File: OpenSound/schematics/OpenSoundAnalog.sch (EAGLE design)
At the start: 60 parts, among them IC2 QUAD_OPAMPD, IC3 TL072D, Q1 BC846, Q2 BC846, Q301 BC846, Q701 BC846

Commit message: changed layout and added Spark Photon footprint
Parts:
- removed CV_A, CV_B: CON-LUMBERG_1502_03, Rebel:CON-LUMBERG_1502_03
- removed IC3: TL072D, linear:TL072D
- removed R1, R3, R4: 1K, resistor:R-EU_R0603
- removed R2: 100R, resistor:R-EU_R0603
- removed R5: 100K, resistor:R-EU_R0603
- removed R6: 10K, resistor:R-EU_R0603
- removed R7: 1M, resistor:R-EU_R0603
- removed R8: 1k, Rebel:R-EU_0603
- removed SV1, SV2: (no value), con-lsta:FE12-1
- removed U$1: MCP4922-E/P, Rebel:MCP4922-E/P
- added CVI1, CVI2: THONKICONN, Rebel:THONKICONN
- added IC1: MCP4822-E/PSOIC8, Rebel:MCP4822-E/PSOIC8
- added R301: 240k, resistor:R-EU_R0603
- added R302: 51k, resistor:R-EU_R0603
- added R303: 33k, resistor:R-EU_R0603
- added R304, R903: 100R, resistor:R-EU_R0603
- added R801: 100K, resistor:R-EU_R0603
- added R802: 1M, resistor:R-EU_R0603
- added R803: 10K, resistor:R-EU_R0603
- added R901, R902, R904: 1K, resistor:R-EU_R0603
- added SPARK: SPARK_CORE, Spark:SPARK_CORECORE
- R504: value 100R -> 1k; device resistor:R-EU_R0603 -> Rebel:R-EU_0603
- renumbered D600 to D200, DAC1 to CVO1, DAC2 to CVO2, R10 to R202, R11 to R203, R604 to R204, R605 to R205, R9 to R201
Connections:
- new net N$12: IC2D.+IN, R301.1, R302.1
- new net N$15: IC2D.-IN, R303.1
- net +12V: now also IC2P.V+, R902.1; no longer IC3P.V+, R4.1
- net +3V3: now also IC1.VDD, R803.1, SPARK.3V3; no longer R6.1, SV1.10, SV1.12, U$1.VDD, U$1.VREFA, U$1.VREFB, U$1.~SHDN
- net +5V: now also SPARK.VIN; no longer SV2.1
- net -12V: now also IC2P.V-, R301.2; no longer IC3P.V-
- net A0: now also SPARK.A0; no longer SV2.12
- net A1: now also SPARK.A1; no longer SV2.11
- net A2: now also IC1.~CS, SPARK.A2; no longer SV2.10, U$1.~CS
- net A3: now also IC1.SCK, SPARK.A3; no longer SV2.9, U$1.SCK
- net A4: now also SPARK.A4; no longer SV2.8
- net A5: now also IC1.SDI, SPARK.A5; no longer SV2.7, U$1.SDI
- net A6: now also SPARK.DAC; no longer SV2.6
- net A7: now also SPARK.WKP; no longer SV2.5
- net D0: now also R901.1, SPARK.D0; no longer R1.1, SV1.1
- net D1: now also SPARK.D1; no longer SV1.2
- net D2: now also R803.2, SPARK.D2; no longer R6.2, SV1.3
- net D3: now also SPARK.D3; no longer SV1.4
- net D4: now also SPARK.D4; no longer SV1.5
- net D5: now also SPARK.D5; no longer SV1.6
- net D6: now also SPARK.D6; no longer SV1.7
- net D7: now also SPARK.D7; no longer SV1.8
- net DAC1: now also IC1.VOUTA; no longer U$1.VOUTA
- net DAC2: now also IC1.VOUTB, R303.2; no longer IC3B.+IN, U$1.VOUTB
- net GND: now also CVI1.4, CVI1.5, CVI2.4, CVI2.5, IC1.AVSS, IC1.~LDAC, IC2C.-IN, R802.2, R904.1, SPARK.GND@2, SPARK.GND@21; no longer CV_A.4, CV_A.5, CV_B.4, CV_B.5, IC3A.+IN, R3.1, R7.2, SV1.9, SV2.2, U$1.AVSS, U$1.~LDAC
- net N$10: now also R801.1; no longer R5.1
- net N$11: now also CVI1.3; no longer CV_A.3
- net N$13: now also IC2C.+IN; no longer IC3A.-IN
- net N$16: now also R504.1; no longer R8.1
- net N$17: now also R504.2; no longer R8.2
- net N$18: now also CVI2.3; no longer CV_B.3
- net N$2: now also R901.2; no longer R1.2
- net N$3: now also IC2D.OUT, R302.2, R304.1; no longer IC3B.-IN, IC3B.OUT, R504.1
- net N$32: now also R304.2; no longer R504.2
- net N$4: now also R902.2, R903.1; no longer R2.1, R4.2
- net N$5: now also R903.2, R904.2; no longer R2.2, R3.2
- net N$7: now also IC2C.OUT; no longer IC3A.OUT
- net N$9: now also R801.2, R802.1; no longer R5.2, R7.1
- net RESET: now also SPARK.!RST; no longer SV1.11
- net RX: now also SPARK.RX; no longer SV2.3
- net TX: now also SPARK.TX; no longer SV2.4
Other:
- moved on the sheet: D500, IC2A, Q1, Q2, Q301, Q701, R501, R502, R503, R504, R505, R601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

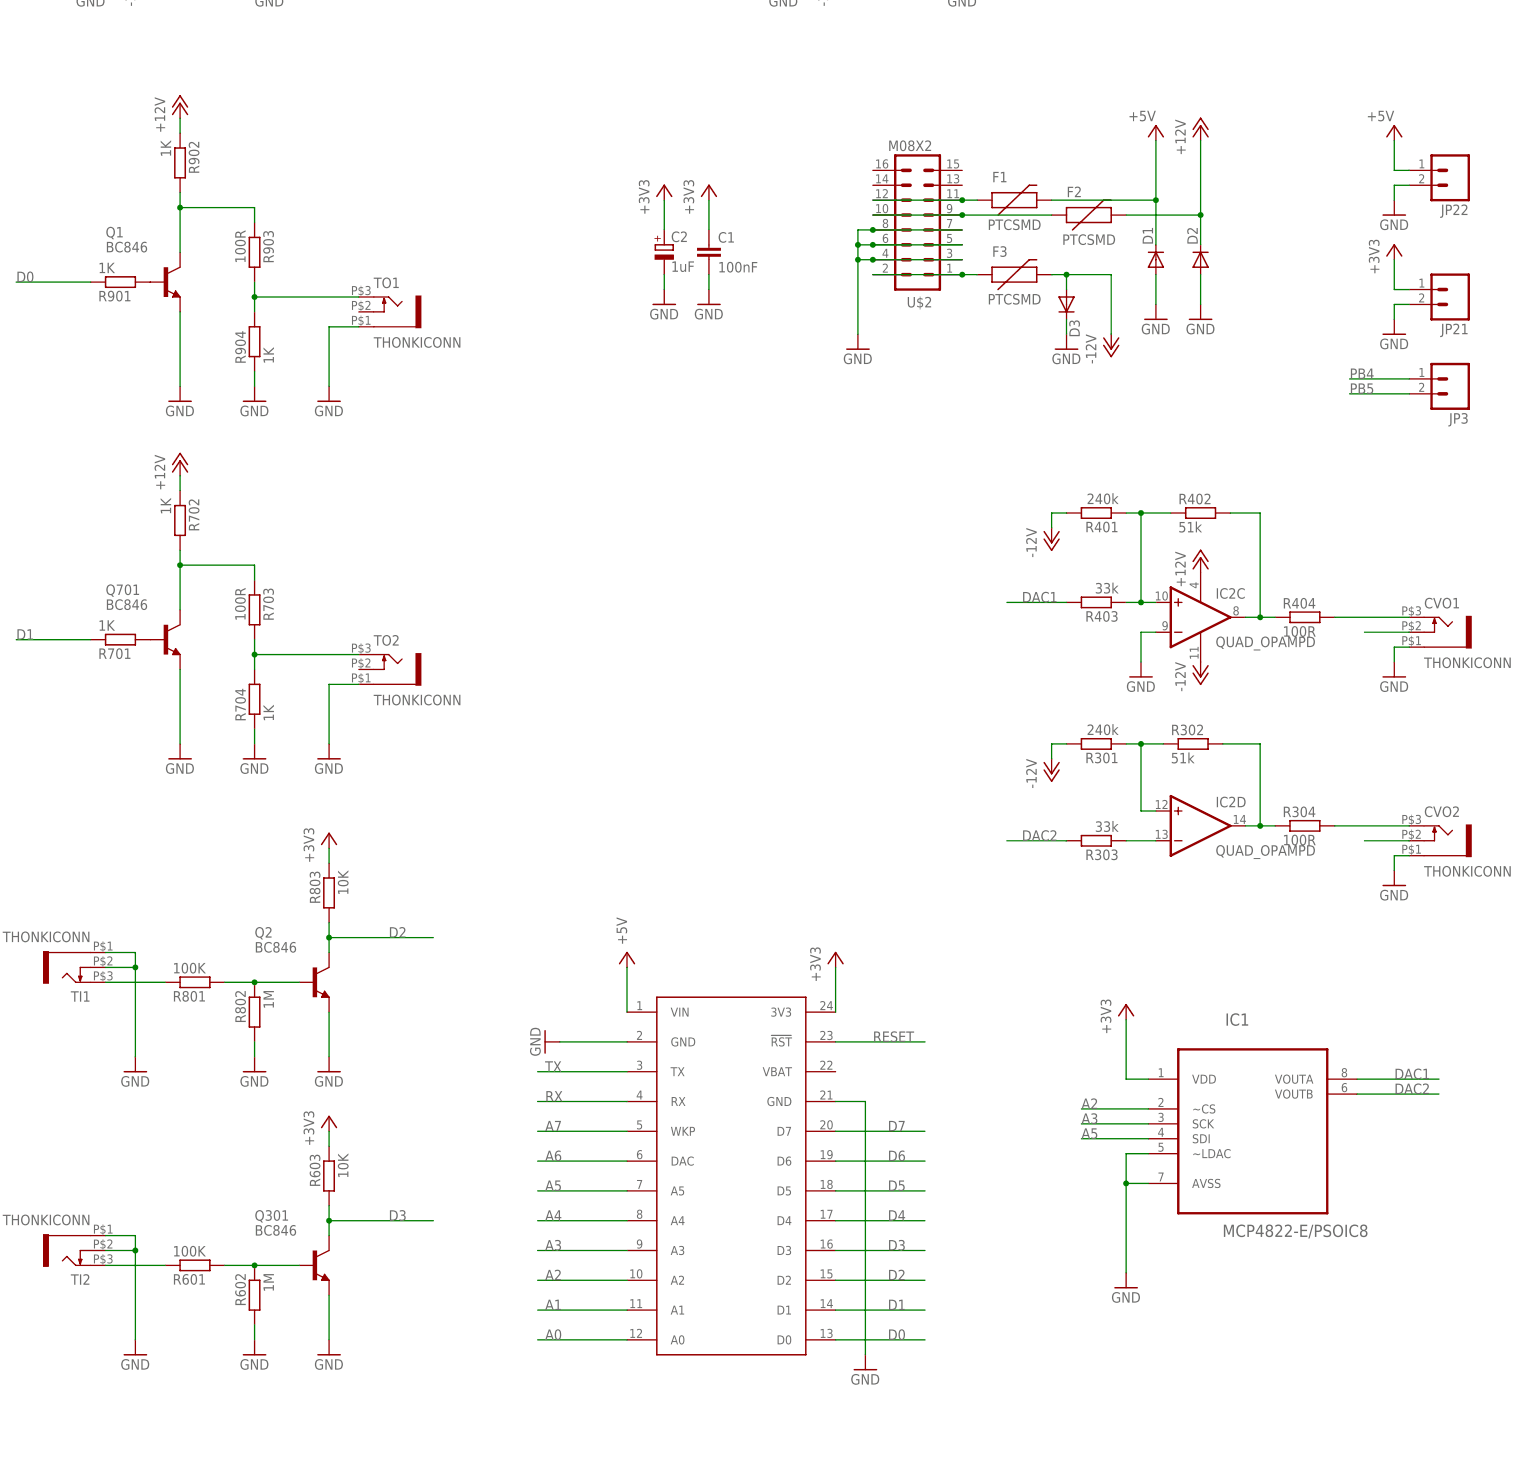
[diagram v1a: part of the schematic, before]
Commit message: added schmitt trigger, fitted components on board
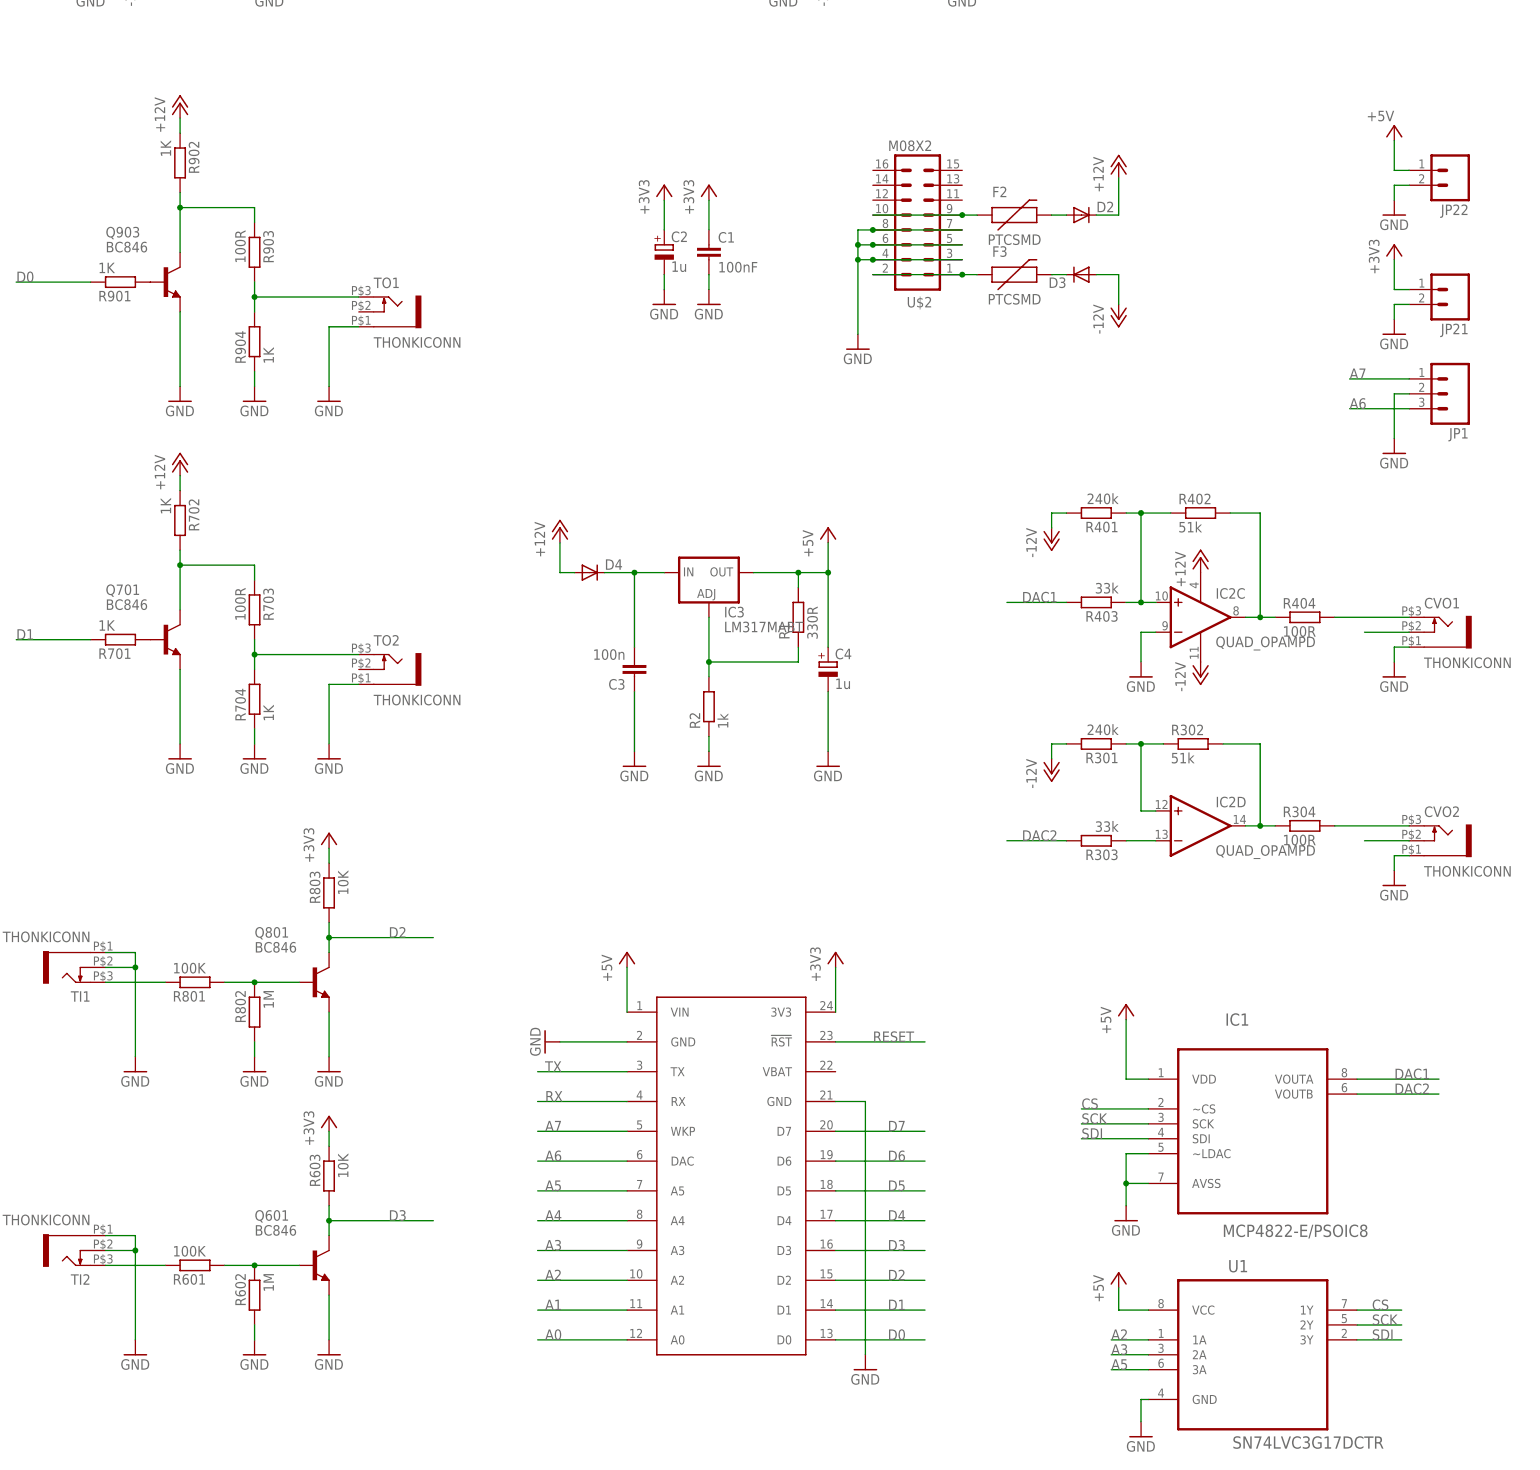
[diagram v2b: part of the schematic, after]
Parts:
- removed D1: (no value), SparkFun:DIODESMA
- removed F1: PTCSMD, SparkFun:PTCSMD
- removed JP3: (no value), SparkFun:M02PTH
- added C3: 100n, rcl:C-EUC0603
- added C4: 1u, rcl:CPOL-EUSANYO_SMD_A5
- added D4: (no value), SparkFun:DIODESMA
- added IC3: LM317MABT, v-reg:LM317MABT
- added JP1: (no value), SparkFun-Connectors:M031X03_NO_SILK
- added R1: 330R, Rebel:R-EU_0603
- added R2: 1k, Rebel:R-EU_0603
- added U1: SN74LVC3G17DCTR, Rebel:SN74LVC3G17DCTR
- C1: device resistor:C-EU050-025X075 -> resistor:C-EUC0603
- C2: value 1uF -> 1u; device resistor:CPOL-EUE5-6 -> rcl:CPOL-EUSANYO_SMD_A5
- R301, R302, R303, R304, R401, R402, R403, R404, R601, R602, R603, R701, R702, R703, R704, R801, R802, R803, R901, R902, R903, R904: device resistor:R-EU_R0603 -> Rebel:R-EU_0603
- renumbered Q1 to Q903, Q2 to Q801, Q301 to Q601
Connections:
- removed net N$44: F1.1, U$2.11, U$2.12
- removed net PB4: JP3.1
- removed net PB5: JP3.2
- new net CS: IC1.~CS, U1.1Y
- new net N$19: IC3.ADJ, R1.1, R2.2
- new net N$21: C3.2, D4.C, IC3.IN
- new net N$25: D3.C, F3.2
- new net N$26: D2.A, F2.2
- new net SCK: IC1.SCK, U1.2Y
- new net SDI: IC1.SDI, U1.3Y
- net +12V: now also D4.A; no longer F2.2
- net +3V3: no longer IC1.VDD
- net +5V: now also C4.+, IC1.VDD, IC3.OUT, R1.2, U1.VCC; no longer D1.C, F1.2
- net -12V: no longer F3.2
- net A2: now also U1.1A; no longer IC1.~CS
- net A3: now also U1.2A; no longer IC1.SCK
- net A5: now also U1.3A; no longer IC1.SDI
- net A6: now also JP1.3
- net A7: now also JP1.1
- net GND: now also C3.1, C4.-, JP1.2, R2.1, U1.GND; no longer D1.A, D2.A, D3.C
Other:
- moved on the sheet: D2, D3, F2

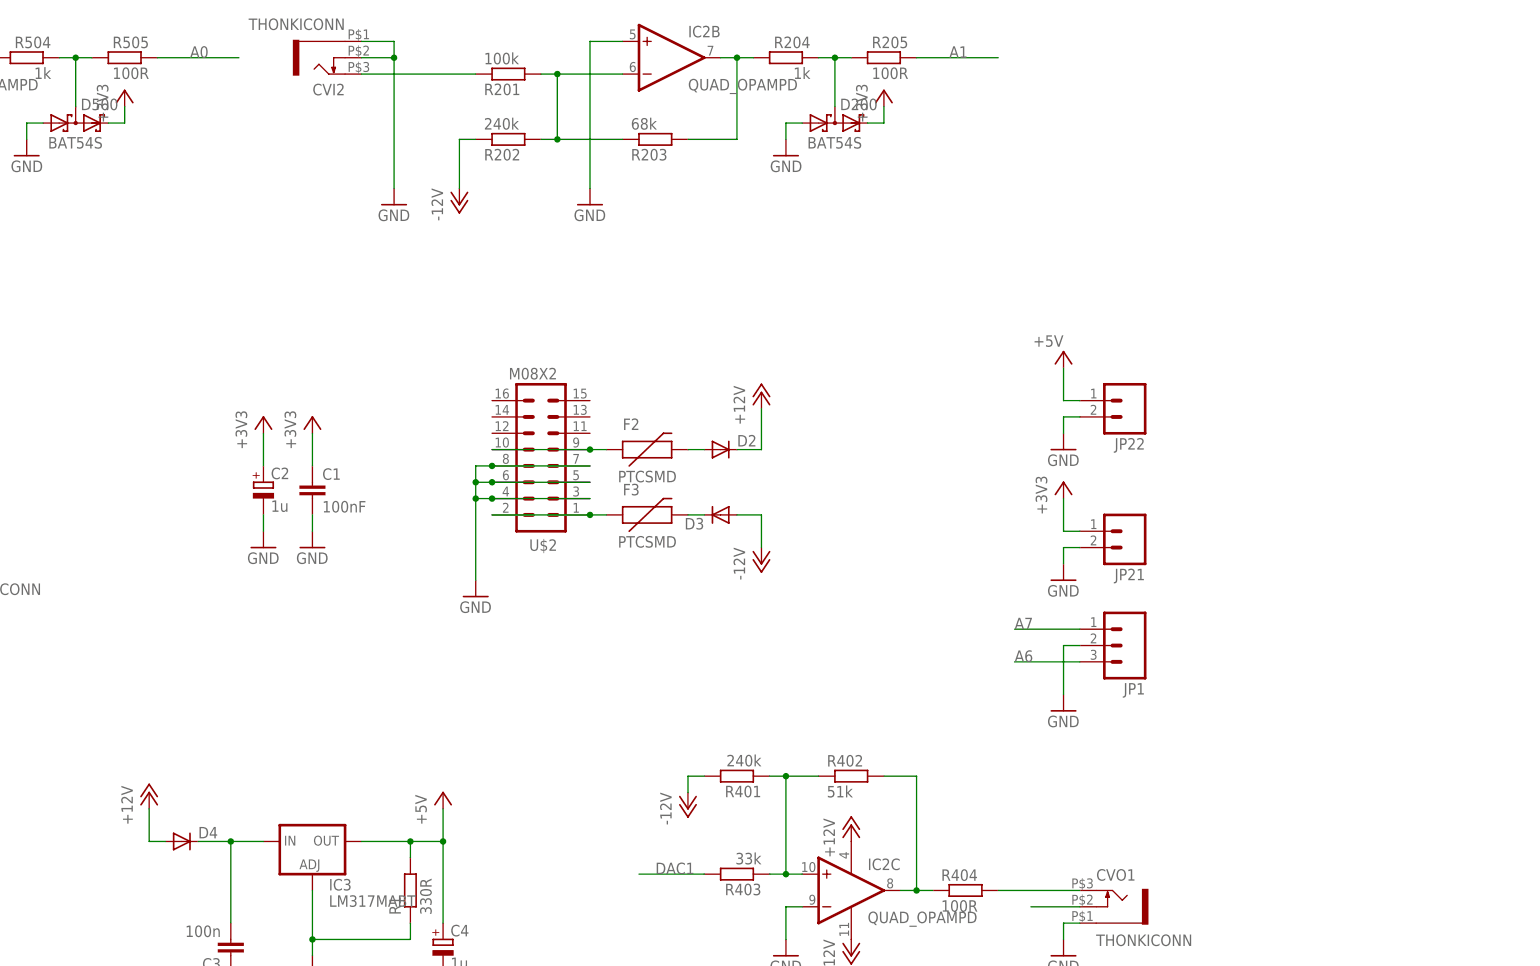
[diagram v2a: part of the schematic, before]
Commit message: added 5GTH9 pushbutton and fitted all on board
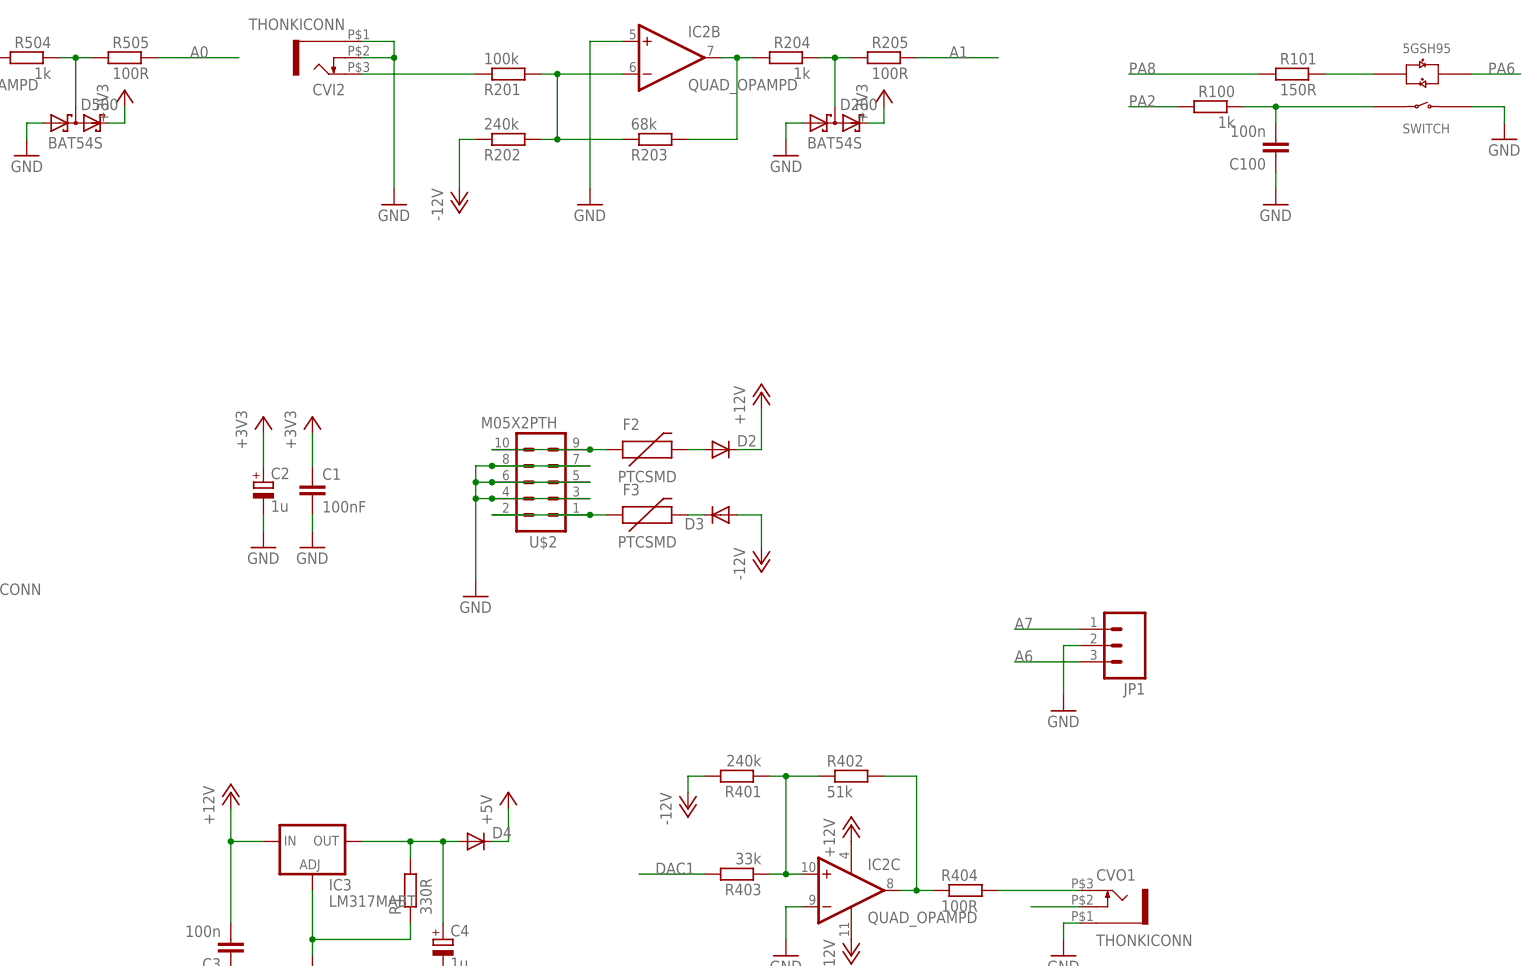
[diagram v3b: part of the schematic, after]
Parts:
- removed JP21, JP22: (no value), SparkFun:M02PTH
- added C100: 100n, rcl:C-EUC0603
- added R100: 1k, Rebel:R-EU_0603
- added R101: 150R, Rebel:R-EU_0603
- added U$1: 5GTH9, SWITCH-5GTH9:5GTH9
- U$2: value M08X2 -> M05X2PTH; device SparkFun:M08X2 -> SparkFun-Connectors:M05X2PTH
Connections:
- new net N$28: R101.1, U$1.LED_G+
- new net PA2: R100.2
- new net PA6: U$1.LED_R+
- new net PA8: R101.2
- new net SWITCH_A: C100.2, R100.1, U$1.SWITCH_A
- net +12V: now also C3.2, IC3.IN; no longer D4.A
- net +3V3: no longer JP21.1
- net +5V: now also D4.C; no longer C4.+, IC3.OUT, JP22.1, R1.2
- net GND: now also C100.1, U$1.SWITCH_B; no longer JP21.2, JP22.2
- net N$21: now also C4.+, D4.A, IC3.OUT, R1.2; no longer C3.2, D4.C, IC3.IN
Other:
- moved on the sheet: D4
